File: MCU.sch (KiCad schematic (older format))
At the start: 25 parts

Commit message: added new TQFP-44 footprint with shorter pads
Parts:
- added R10: 500, symbol Device:R
- gave numbers to parts that had none: 25
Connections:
- net RC2B: no longer U1.12 (PB7)
- net RGB_DIN: now also R10.1; no longer U1.32 (PC7)
- net at U1.39 (PF4): now also R10.2
- new net Backlight: U1.12 (PB7)

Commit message: added new generic SMD pad footprints and footprint associations
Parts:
- C17, C18, C19, C21: footprint (none) -> Capacitor_SMD:C_0805_2012Metric
- D27, D28, D29: footprint (none) -> Diode_SMD:D_SMA
- F1: footprint (none) -> Fuse:Fuse_1812_4532Metric
- J1: footprint (none) -> keebio:HRO-TYPE-C-31-M-12-Assembly
- J8: footprint (none) -> Connector_PinHeader_2.54mm:PinHeader_2x03_P2.54mm_Vertical
- NT1: footprint (none) -> NetTie:NetTie-2_SMD_Pad2.0mm
- R10, R3, R4, R5, R6, R7: footprint (none) -> Resistor_SMD:R_0805_2012Metric
- Y1: footprint (none) -> Resistor_SMD:R_1210_3225Metric
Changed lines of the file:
@@
 F 0 "NT1" H 800 4900 50  0000 C CNN
 F 1 "Net-Tie_2" H 800 5000 50  0000 C CNN
-F 2 "" H 1000 5050 50  0001 C CNN
+F 2 "NetTie:NetTie-2_SMD_Pad2.0mm" H 1000 5050 50  0001 C CNN
 F 3 "~" H 1000 5050 50  0001 C CNN
 	1    1000 5050
@@
 F 0 "R6" V 2240 2700 50  0000 C CNN
 F 1 "22" V 2333 2700 50  0000 C CNN
-F 2 "" V 2380 2700 50  0001 C CNN
+F 2 "Resistor_SMD:R_0805_2012Metric" V 2380 2700 50  0001 C CNN
 F 3 "~" H 2450 2700 50  0001 C CNN
 	1    2450 2700
@@
 F 0 "R7" V 2550 2900 50  0000 C CNN
 F 1 "22" V 2650 2900 50  0000 C CNN
-F 2 "" V 2380 2900 50  0001 C CNN
+F 2 "Resistor_SMD:R_0805_2012Metric" V 2380 2900 50  0001 C CNN
 F 3 "~" H 2450 2900 50  0001 C CNN
 	1    2450 2900
@@
 F 0 "C17" H 3565 2397 50  0000 L CNN
 F 1 "1 uF" H 3565 2304 50  0000 L CNN
-F 2 "" H 3488 2200 50  0001 C CNN
+F 2 "Capacitor_SMD:C_0805_2012Metric" H 3488 2200 50  0001 C CNN
 F 3 "~" H 3450 2350 50  0001 C CNN
 	1    3450 2350
@@
 F 0 "C21" H 5115 3747 50  0000 L CNN
 F 1 "1 uF" H 5115 3654 50  0000 L CNN
-F 2 "" H 5038 3550 50  0001 C CNN
+F 2 "Capacitor_SMD:C_0805_2012Metric" H 5038 3550 50  0001 C CNN
 F 3 "~" H 5000 3700 50  0001 C CNN
 	1    5000 3700
@@
 F 0 "Y1" V 4753 2539 50  0000 L CNN
 F 1 "16 MHz" V 4846 2539 50  0000 L CNN
-F 2 "" H 4800 2450 50  0001 C CNN
+F 2 "Resistor_SMD:R_1210_3225Metric" H 4800 2450 50  0001 C CNN
 F 3 "~" H 4800 2450 50  0001 C CNN
 	1    4800 2450
@@
 F 0 "C18" V 4400 2200 50  0000 C CNN
 F 1 "22 pF" V 4400 2550 50  0000 C CNN
-F 2 "" H 4538 2200 50  0001 C CNN
+F 2 "Capacitor_SMD:C_0805_2012Metric" H 4538 2200 50  0001 C CNN
 F 3 "~" H 4500 2350 50  0001 C CNN
 	1    4500 2350
@@
 F 0 "C19" V 4600 2400 50  0000 C CNN
 F 1 "22 pF" V 4600 2750 50  0000 C CNN
-F 2 "" H 4538 2400 50  0001 C CNN
+F 2 "Capacitor_SMD:C_0805_2012Metric" H 4538 2400 50  0001 C CNN
 F 3 "~" H 4500 2550 50  0001 C CNN
 	1    4500 2550
@@
 F 0 "R5" V 2900 2300 50  0000 C CNN
 F 1 "5.1k" V 2900 2500 50  0000 C CNN
-F 2 "" V 2730 2400 50  0001 C CNN
+F 2 "Resistor_SMD:R_0805_2012Metric" V 2730 2400 50  0001 C CNN
 F 3 "~" H 2800 2400 50  0001 C CNN
 	1    2800 2400
@@
 F 0 "R4" V 2700 2200 50  0000 C CNN
 F 1 "5.1k" V 2700 2400 50  0000 C CNN
-F 2 "" V 2730 2300 50  0001 C CNN
+F 2 "Resistor_SMD:R_0805_2012Metric" V 2730 2300 50  0001 C CNN
 F 3 "~" H 2800 2300 50  0001 C CNN
 	1    2800 2300
@@
 F 0 "J8" H 1850 6470 50  0000 C CNN
 F 1 "ISP Header" H 1850 6377 50  0000 C CNN
-F 2 "" H 1800 6150 50  0001 C CNN
+F 2 "Connector_PinHeader_2.54mm:PinHeader_2x03_P2.54mm_Vertical" H 1800 6150 50  0001 C CNN
 F 3 "~" H 1800 6150 50  0001 C CNN
 	1    1800 6150
@@
 F 0 "F1" V 2271 2100 50  0000 C CNN
 F 1 "Polyfuse 500 mA" V 2364 2100 50  0000 C CNN
-F 2 "" H 2550 1900 50  0001 L CNN
+F 2 "Fuse:Fuse_1812_4532Metric" H 2550 1900 50  0001 L CNN
 F 3 "~" H 2500 2100 50  0001 C CNN
 	1    2500 2100
@@
 F 0 "D27" V 1853 4729 50  0000 L CNN
 F 1 "D_TVS" V 1946 4729 50  0000 L CNN
-F 2 "" H 1900 4650 50  0001 C CNN
+F 2 "Diode_SMD:D_SMA" H 1900 4650 50  0001 C CNN
 F 3 "~" H 1900 4650 50  0001 C CNN
 	1    1900 4650
@@
 F 0 "D28" V 2253 4729 50  0000 L CNN
 F 1 "D_TVS" V 2346 4729 50  0000 L CNN
-F 2 "" H 2300 4650 50  0001 C CNN
+F 2 "Diode_SMD:D_SMA" H 2300 4650 50  0001 C CNN
 F 3 "~" H 2300 4650 50  0001 C CNN
 	1    2300 4650
@@
 F 0 "D29" V 2653 4729 50  0000 L CNN
 F 1 "D_TVS" V 2746 4729 50  0000 L CNN
-F 2 "" H 2700 4650 50  0001 C CNN
+F 2 "Diode_SMD:D_SMA" H 2700 4650 50  0001 C CNN
 F 3 "~" H 2700 4650 50  0001 C CNN
 	1    2700 4650
@@
 F 0 "R3" V 5250 1900 50  0000 C CNN
 F 1 "5.1k" V 5350 1900 50  0000 C CNN
-F 2 "" V 5080 1900 50  0001 C CNN
+F 2 "Resistor_SMD:R_0805_2012Metric" V 5080 1900 50  0001 C CNN
 F 3 "~" H 5150 1900 50  0001 C CNN
 	1    5150 1900
@@
 F 0 "R10" V 6740 4750 50  0000 C CNN
 F 1 "500" V 6833 4750 50  0000 C CNN
-F 2 "" V 6880 4750 50  0001 C CNN
+F 2 "Resistor_SMD:R_0805_2012Metric" V 6880 4750 50  0001 C CNN
 F 3 "~" H 6950 4750 50  0001 C CNN
 	1    6950 4750
@@
 F 0 "J1" H 1207 4370 50  0000 C CNN
 F 1 "USB_C_Receptacle" H 1207 4277 50  0000 C CNN
-F 2 "" H 1250 3100 50  0001 C CNN
+F 2 "keebio:HRO-TYPE-C-31-M-12-Assembly" H 1250 3100 50  0001 C CNN
 F 3 "https://www.usb.org/sites/default/files/documents/usb_type-c.zip" H 1250 3100 50  0001 C CNN
 	1    1100 3100

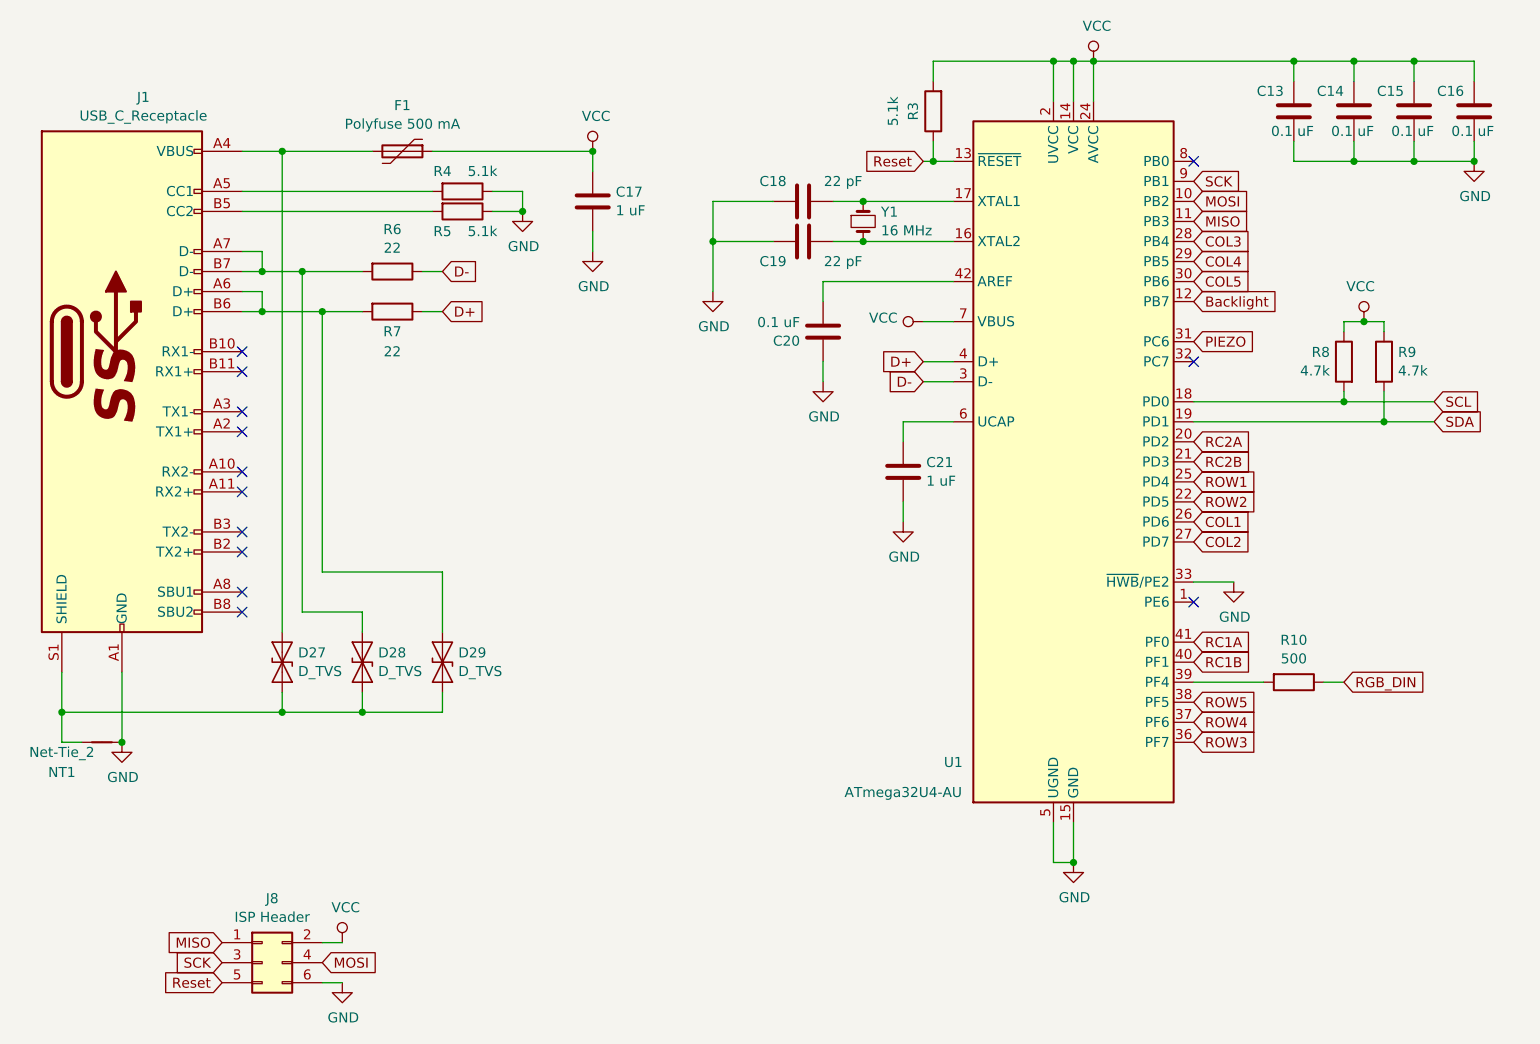
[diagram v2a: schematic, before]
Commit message: new component annotations
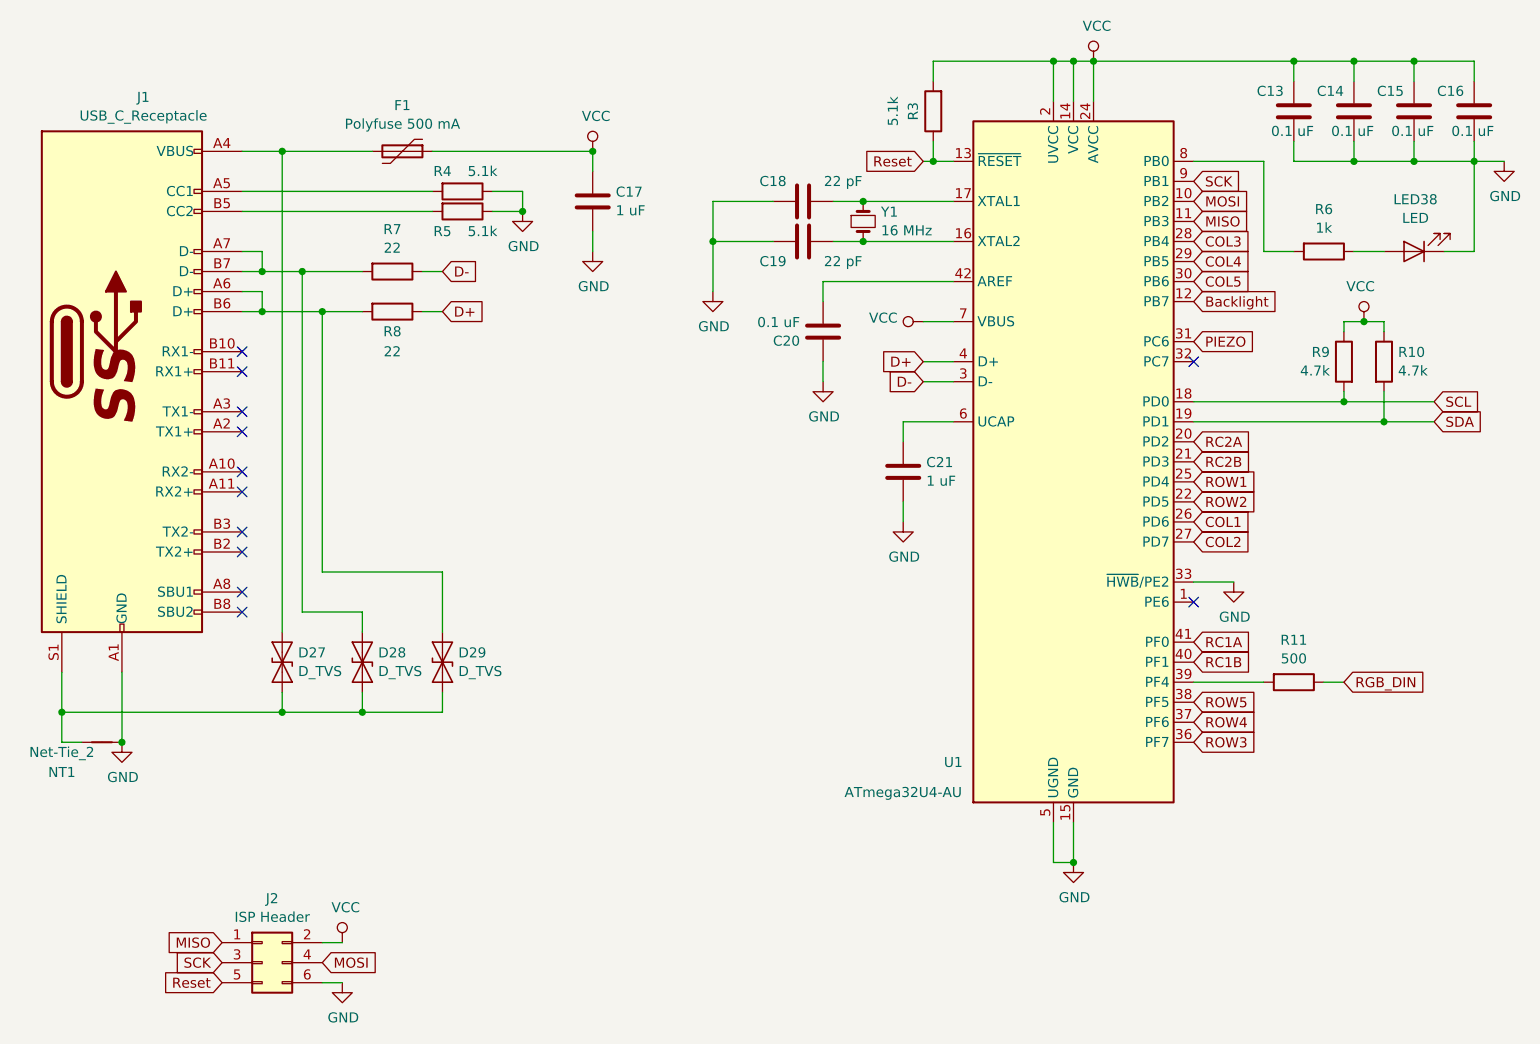
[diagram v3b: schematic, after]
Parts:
- added LED38: LED, LED_SMD:LED_0805_2012Metric, symbol Device:LED
- added R6: 1k, Resistor_SMD:R_0805_2012Metric, symbol Device:R
- renumbered J8 to J2, R9 to R10, R10 to R11, R6 to R7, R7 to R8, R8 to R9
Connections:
- net GND: now also LED38.1 (K)
- net at U1.8 (PB0): now also R6.2
- new net: LED38.2 (A), R6.1
- no-connect marks 13 -> 12
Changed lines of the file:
@@
 	800  5050 900  5050
 $Comp
-L power:GND #PWR058
+L power:GND #PWR060
 U 1 1 5D7C7FBD
 P 1100 5050
-F 0 "#PWR058" H 1100 4800 50  0001 C CNN
+F 0 "#PWR060" H 1100 4800 50  0001 C CNN
 F 1 "GND" H 1105 4875 50  0000 C CNN
 F 2 "" H 1100 5050 50  0001 C CNN
@@
 Connection ~ 1100 5050
 $Comp
-L Device:R R6
+L Device:R R7
 U 1 1 5D7C9C2B
 P 2450 2700
-F 0 "R6" V 2240 2700 50  0000 C CNN
+F 0 "R7" V 2240 2700 50  0000 C CNN
 F 1 "22" V 2333 2700 50  0000 C CNN
 F 2 "Resistor_SMD:R_0805_2012Metric" V 2380 2700 50  0001 C CNN
@@
 Connection ~ 1800 2700
 $Comp
-L Device:R R7
+L Device:R R8
 U 1 1 5D7CCF4C
 P 2450 2900
-F 0 "R7" V 2550 2900 50  0000 C CNN
+F 0 "R8" V 2550 2900 50  0000 C CNN
 F 1 "22" V 2650 2900 50  0000 C CNN
 F 2 "Resistor_SMD:R_0805_2012Metric" V 2380 2900 50  0001 C CNN
@@
 	5850 5650 5850 5450
 $Comp
-L power:GND #PWR059
+L power:GND #PWR061
 U 1 1 5D7D0F0A
 P 5850 5650
-F 0 "#PWR059" H 5850 5400 50  0001 C CNN
+F 0 "#PWR061" H 5850 5400 50  0001 C CNN
 F 1 "GND" H 5855 5475 50  0000 C CNN
 F 2 "" H 5850 5650 50  0001 C CNN
@@
 	5950 1650 5950 1850
 $Comp
-L power:VCC #PWR047
+L power:VCC #PWR049
 U 1 1 5D7D2B34
 P 5950 1650
-F 0 "#PWR047" H 5950 1500 50  0001 C CNN
+F 0 "#PWR049" H 5950 1500 50  0001 C CNN
 F 1 "VCC" H 5967 1825 50  0000 C CNN
 F 2 "" H 5950 1650 50  0001 C CNN
@@
 Connection ~ 5850 1650
 $Comp
-L power:VCC #PWR048
+L power:VCC #PWR050
 U 1 1 5D7DBA0E
 P 3450 2100
-F 0 "#PWR048" H 3450 1950 50  0001 C CNN
+F 0 "#PWR050" H 3450 1950 50  0001 C CNN
 F 1 "VCC" H 3467 2275 50  0000 C CNN
 F 2 "" H 3450 2100 50  0001 C CNN
@@
 $EndComp
 $Comp
-L power:GND #PWR051
+L power:GND #PWR053
 U 1 1 5D7DC098
 P 3450 2600
-F 0 "#PWR051" H 3450 2350 50  0001 C CNN
+F 0 "#PWR053" H 3450 2350 50  0001 C CNN
 F 1 "GND" H 3455 2425 50  0000 C CNN
 F 2 "" H 3450 2600 50  0001 C CNN
@@
 	5100 2150 5150 2150
 $Comp
-L power:VCC #PWR053
+L power:VCC #PWR055
 U 1 1 5D7E5EFD
 P 5100 2950
-F 0 "#PWR053" H 5100 2800 50  0001 C CNN
+F 0 "#PWR055" H 5100 2800 50  0001 C CNN
 F 1 "VCC" V 5118 3078 50  0000 L CNN
 F 2 "" H 5100 2950 50  0001 C CNN
@@
 $EndComp
 $Comp
-L power:GND #PWR055
+L power:GND #PWR057
 U 1 1 5D7F0A14
 P 4600 3250
-F 0 "#PWR055" H 4600 3000 50  0001 C CNN
+F 0 "#PWR057" H 4600 3000 50  0001 C CNN
 F 1 "GND" H 4605 3075 50  0000 C CNN
 F 2 "" H 4600 3250 50  0001 C CNN
@@
 	5000 3450 5250 3450
 $Comp
-L power:GND #PWR056
+L power:GND #PWR058
 U 1 1 5D7F5072
 P 5000 3950
-F 0 "#PWR056" H 5000 3700 50  0001 C CNN
+F 0 "#PWR058" H 5000 3700 50  0001 C CNN
 F 1 "GND" H 5005 3775 50  0000 C CNN
 F 2 "" H 5000 3950 50  0001 C CNN
@@
 Connection ~ 4800 2550
 $Comp
-L power:GND #PWR052
+L power:GND #PWR054
 U 1 1 5D80A271
 P 4050 2800
-F 0 "#PWR052" H 4050 2550 50  0001 C CNN
+F 0 "#PWR054" H 4050 2550 50  0001 C CNN
 F 1 "GND" H 4055 2625 50  0000 C CNN
 F 2 "" H 4050 2800 50  0001 C CNN
@@
 	4050 2550 4050 2800
 $Comp
-L power:GND #PWR057
+L power:GND #PWR059
 U 1 1 5D80EFB3
 P 6650 4250
-F 0 "#PWR057" H 6650 4000 50  0001 C CNN
+F 0 "#PWR059" H 6650 4000 50  0001 C CNN
 F 1 "GND" H 6655 4075 50  0000 C CNN
 F 2 "" H 6650 4250 50  0001 C CNN
@@
 $EndComp
 $Comp
-L power:GND #PWR050
+L power:GND #PWR052
 U 1 1 5D830369
 P 3100 2400
-F 0 "#PWR050" H 3100 2150 50  0001 C CNN
+F 0 "#PWR052" H 3100 2150 50  0001 C CNN
 F 1 "GND" H 3105 2225 50  0000 C CNN
 F 2 "" H 3100 2400 50  0001 C CNN
@@
 P 7300 2950
 AR Path="/5D863561" Ref="#PWR?"  Part="1"
-AR Path="/5D7850B4/5D863561" Ref="#PWR054"  Part="1"
-F 0 "#PWR054" H 7300 2800 50  0001 C CNN
+AR Path="/5D7850B4/5D863561" Ref="#PWR056"  Part="1"
+F 0 "#PWR056" H 7300 2800 50  0001 C CNN
 F 1 "VCC" H 7317 3125 50  0000 C CNN
 F 2 "" H 7300 2950 50  0001 C CNN
@@
 P 7200 3150
 AR Path="/5D86356C" Ref="R?"  Part="1"
-AR Path="/5D7850B4/5D86356C" Ref="R8"  Part="1"
-F 0 "R8" H 7270 3197 50  0000 L CNN
+AR Path="/5D7850B4/5D86356C" Ref="R9"  Part="1"
+F 0 "R9" H 7270 3197 50  0000 L CNN
 F 1 "4.7k" H 7270 3104 50  0000 L CNN
 F 2 "Resistor_SMD:R_0805_2012Metric" V 7130 3150 50  0001 C CNN
@@
 P 7400 3150
 AR Path="/5D863572" Ref="R?"  Part="1"
-AR Path="/5D7850B4/5D863572" Ref="R9"  Part="1"
-F 0 "R9" H 7470 3197 50  0000 L CNN
+AR Path="/5D7850B4/5D863572" Ref="R10"  Part="1"
+F 0 "R10" H 7470 3197 50  0000 L CNN
 F 1 "4.7k" H 7470 3104 50  0000 L CNN
 F 2 "Resistor_SMD:R_0805_2012Metric" V 7330 3150 50  0001 C CNN
@@
 	7550 2150 7850 2150
 $Comp
-L power:GND #PWR049
+L power:GND #PWR051
 U 1 1 5D884781
-P 7850 2150
-F 0 "#PWR049" H 7850 1900 50  0001 C CNN
-F 1 "GND" H 7855 1975 50  0000 C CNN
-F 2 "" H 7850 2150 50  0001 C CNN
-F 3 "" H 7850 2150 50  0001 C CNN
-	1    7850 2150
+P 8000 2150
+F 0 "#PWR051" H 8000 1900 50  0001 C CNN
+F 1 "GND" H 8005 1975 50  0000 C CNN
+F 2 "" H 8000 2150 50  0001 C CNN
+F 3 "" H 8000 2150 50  0001 C CNN
+	1    8000 2150
 	1    0    0    -1
 $EndComp
 Connection ~ 7850 2150
 $Comp
-L Connector_Generic:Conn_02x03_Odd_Even J8
+L Connector_Generic:Conn_02x03_Odd_Even J2
 U 1 1 5D8967C3
 P 1800 6150
-F 0 "J8" H 1850 6470 50  0000 C CNN
+F 0 "J2" H 1850 6470 50  0000 C CNN
 F 1 "ISP Header" H 1850 6377 50  0000 C CNN
 F 2 "Connector_PinHeader_2.54mm:PinHeader_2x03_P2.54mm_Vertical" H 1800 6150 50  0001 C CNN
@@
 	1100 4700 1100 5050
 $Comp
-L power:GND #PWR061
+L power:GND #PWR063
 U 1 1 5D92AEC7
 P 2200 6250
-F 0 "#PWR061" H 2200 6000 50  0001 C CNN
+F 0 "#PWR063" H 2200 6000 50  0001 C CNN
 F 1 "GND" H 2205 6075 50  0000 C CNN
 F 2 "" H 2200 6250 50  0001 C CNN
@@
 	2100 6050 2200 6050
 $Comp
-L power:VCC #PWR060
+L power:VCC #PWR062
 U 1 1 5D932F5C
 P 2200 6050
-F 0 "#PWR060" H 2200 5900 50  0001 C CNN
+F 0 "#PWR062" H 2200 5900 50  0001 C CNN
 F 1 "VCC" H 2217 6225 50  0000 C CNN
 F 2 "" H 2200 6050 50  0001 C CNN
@@
 $EndComp
 NoConn ~ 6450 4350
-NoConn ~ 6450 2150
 $Comp
 L MCU_Microchip_ATmega:ATmega32U4-AU U?
@@
 NoConn ~ 6450 3150
 $Comp
-L Device:R R10
+L Device:R R11
 U 1 1 5D781429
 P 6950 4750
-F 0 "R10" V 6740 4750 50  0000 C CNN
+F 0 "R11" V 6740 4750 50  0000 C CNN
 F 1 "500" V 6833 4750 50  0000 C CNN
 F 2 "Resistor_SMD:R_0805_2012Metric" V 6880 4750 50  0001 C CNN
@@
 	1    0    0    -1
 $EndComp
+Wire Wire Line
+	6450 2150 6800 2150
+$Comp
+L Device:R R6
+U 1 1 5D77E898
+P 7100 2600
+F 0 "R6" V 6890 2600 50  0000 C CNN
+F 1 "1k" V 6983 2600 50  0000 C CNN
+F 2 "Resistor_SMD:R_0805_2012Metric" V 7030 2600 50  0001 C CNN
+F 3 "~" H 7100 2600 50  0001 C CNN
+	1    7100 2600
+	0    1    1    0
+$EndComp
+$Comp
+L Device:LED LED38
+U 1 1 5D77F6B8
+P 7550 2600
+F 0 "LED38" H 7543 2341 50  0000 C CNN
+F 1 "LED" H 7543 2434 50  0000 C CNN
+F 2 "LED_SMD:LED_0805_2012Metric" H 7550 2600 50  0001 C CNN
+F 3 "~" H 7550 2600 50  0001 C CNN
+	1    7550 2600
+	-1   0    0    1
+$EndComp
+Wire Wire Line
+	6800 2600 6950 2600
+Wire Wire Line
+	6800 2150 6800 2600
+Wire Wire Line
+	7250 2600 7400 2600
+Wire Wire Line
+	7700 2600 7850 2600
+Wire Wire Line
+	7850 2600 7850 2150
+Wire Wire Line
+	7850 2150 8000 2150
 $EndSCHEMATC

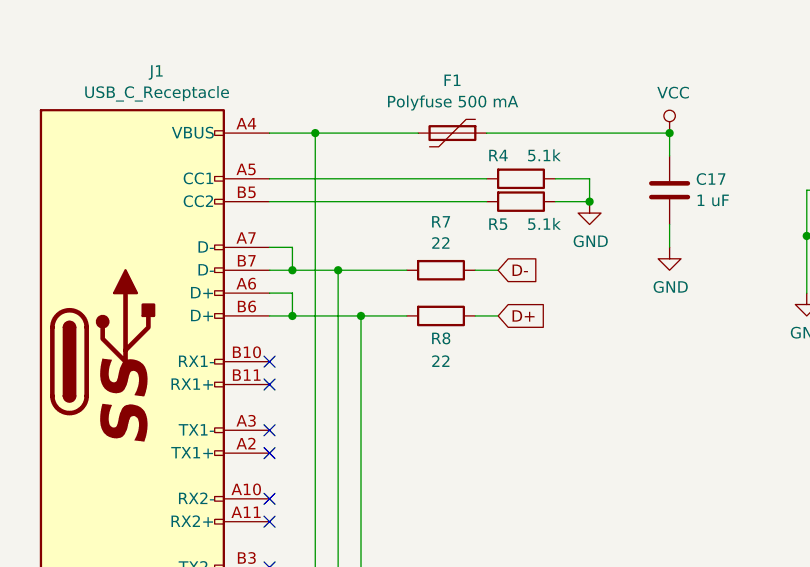
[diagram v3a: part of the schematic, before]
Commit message: initial pcb layout and schematic optimizations
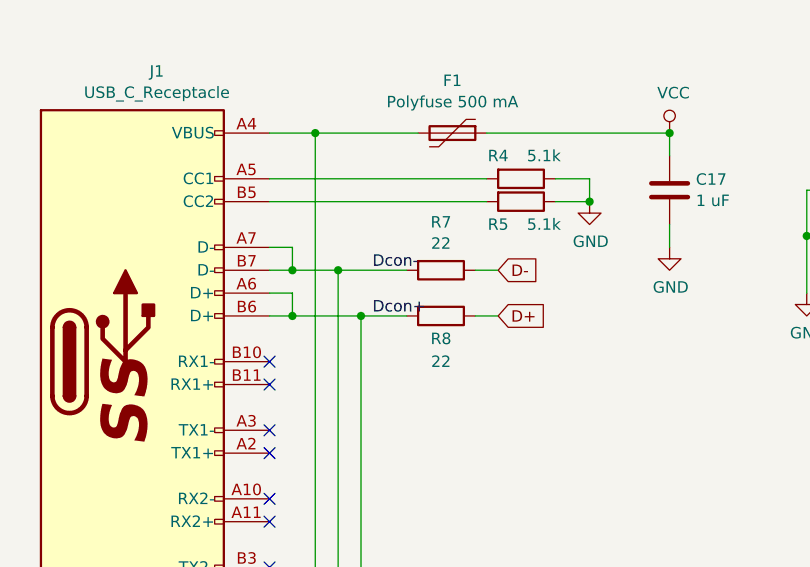
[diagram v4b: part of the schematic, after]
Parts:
- J1: footprint keebio:HRO-TYPE-C-31-M-12-Assembly -> testatur:HRO-TYPE-C-31-M-12_kicad-pinout
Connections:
- net Dcon+: now reaches D29.1 (A1), J1.A6 (D+), J1.B6 (D+), R8.2
- net Dcon-: now reaches D28.1 (A1), J1.A7 (D-), J1.B7 (D-), R7.2
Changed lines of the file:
@@
 F 0 "J1" H 1207 4370 50  0000 C CNN
 F 1 "USB_C_Receptacle" H 1207 4277 50  0000 C CNN
-F 2 "keebio:HRO-TYPE-C-31-M-12-Assembly" H 1250 3100 50  0001 C CNN
+F 2 "testatur:HRO-TYPE-C-31-M-12_kicad-pinout" H 1250 3100 50  0001 C CNN
 F 3 "https://www.usb.org/sites/default/files/documents/usb_type-c.zip" H 1250 3100 50  0001 C CNN
 	1    1100 3100
@@
 Wire Wire Line
 	7850 2150 8000 2150
+Text Label 2150 2700 0    50   ~ 0
+Dcon-
+Text Label 2150 2900 0    50   ~ 0
+Dcon+
 $EndSCHEMATC
